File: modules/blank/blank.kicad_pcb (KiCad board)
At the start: 2 copper layers, 27.9 x 66 mm, 2 parts

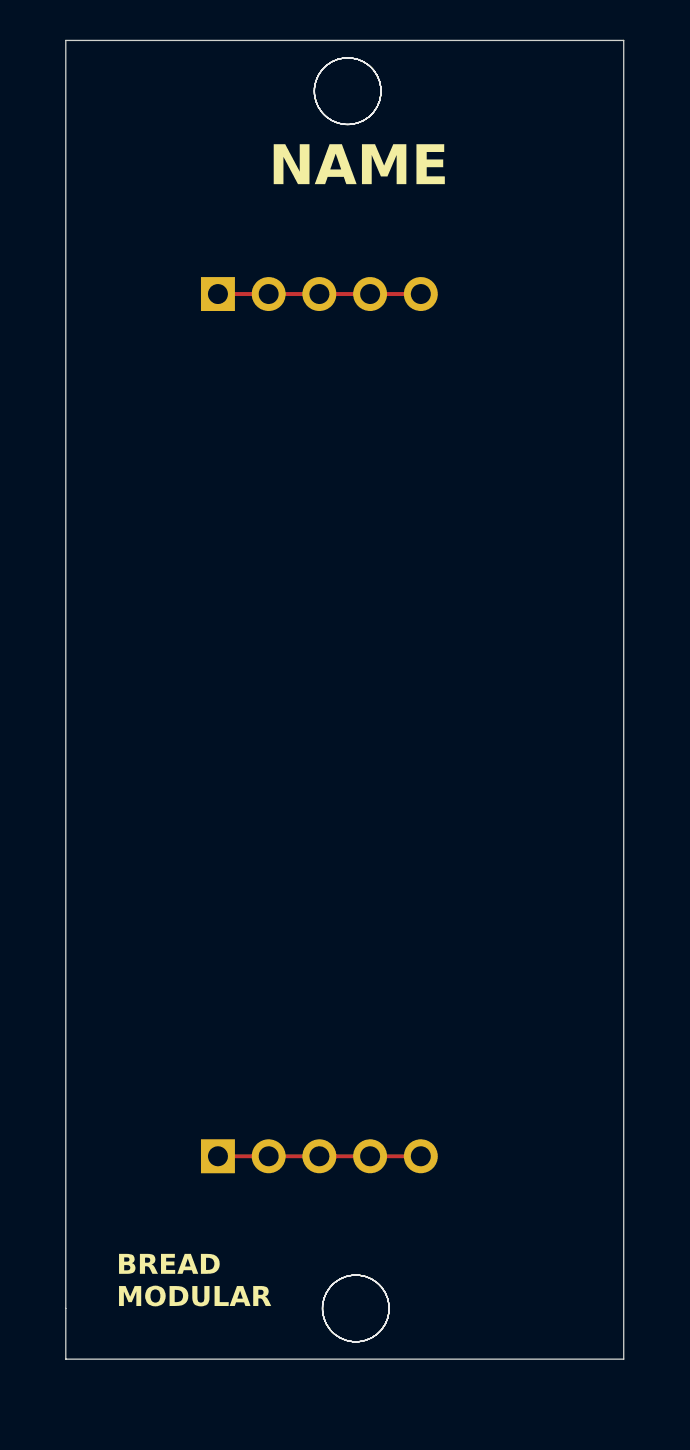
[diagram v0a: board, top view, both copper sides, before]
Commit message: Retouched the Blank Module with new sizes.
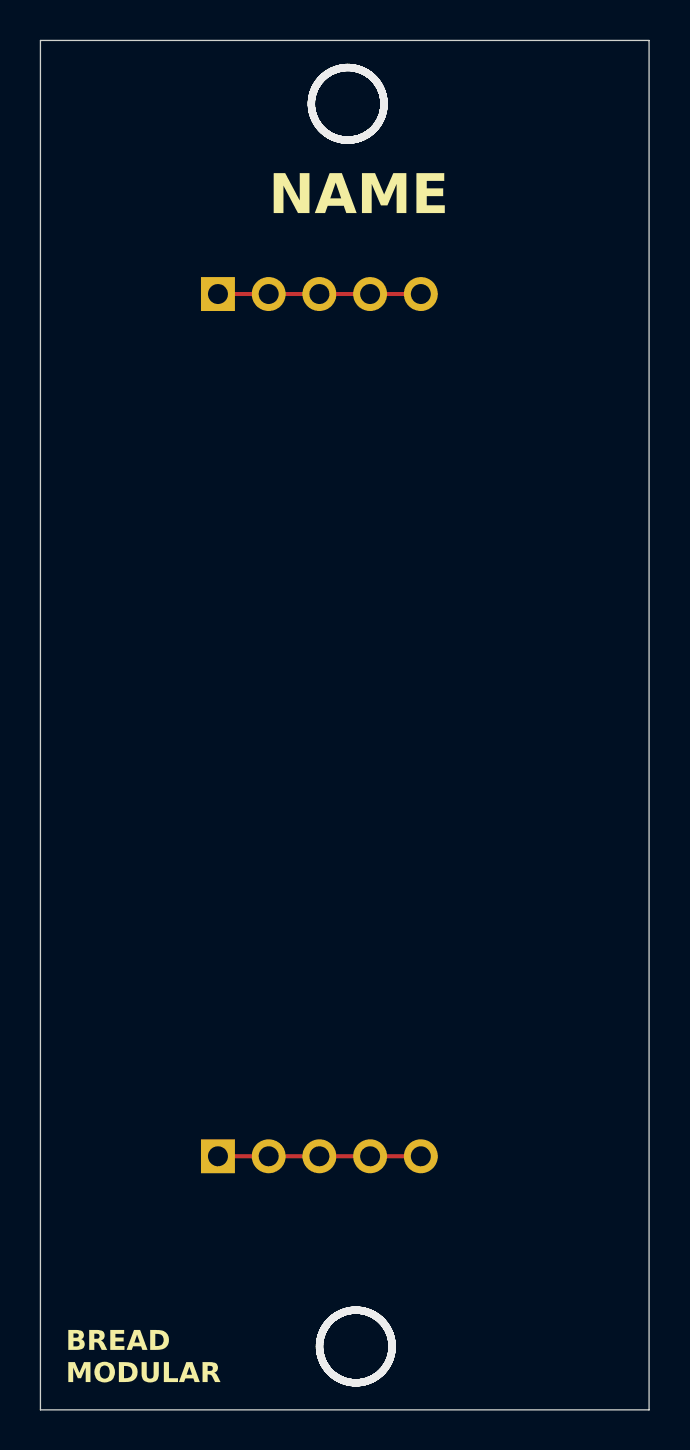
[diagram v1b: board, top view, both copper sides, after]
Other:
- board size 27.9 x 66 mm -> 30.5 x 68.6 mm
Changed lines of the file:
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@@
 	)
 	(gr_line
-		(start 48.26 106.68)
-		(end 76.2 106.68)
+		(start 46.99 109.22)
+		(end 77.47 109.22)
 		(stroke
 			(width 0.05)
@@
 	)
 	(gr_line
-		(start 48.26 104.14)
-		(end 48.26 106.68)
+		(start 77.47 40.64)
+		(end 46.99 40.64)
 		(stroke
 			(width 0.05)
@@
 	)
 	(gr_line
-		(start 76.2 40.64)
-		(end 48.26 40.64)
+		(start 46.99 40.64)
+		(end 46.99 109.22)
 		(stroke
 			(width 0.05)
@@
 	)
 	(gr_line
-		(start 48.26 40.64)
-		(end 48.26 104.14)
-		(stroke
-			(width 0.05)
-			(type default)
-		)
-		(layer "Edge.Cuts")
-	)
-	(gr_line
-		(start 76.2 106.68)
-		(end 76.2 40.64)
+		(start 77.47 109.22)
+		(end 77.47 40.64)
 		(stroke
 			(width 0.05)
@@
 	)
 	(gr_text "NAME"
-		(at 58.42 48.081611 0)
+		(at 58.42 49.53 0)
 		(layer "F.SilkS")
 		(effects
@@
 	)
 	(gr_text "BREAD\nMODULAR"
-		(at 50.8 104.14 0)
+		(at 48.26 107.95 0)
 		(layer "F.SilkS")
 		(effects
@@
 	)
 	(via
-		(at 62.37758 43.18)
-		(size 3.4)
+		(at 62.37758 43.815)
+		(size 4)
 		(drill 3.2)
 		(layers "F.Cu" "B.Cu")
@@
 	)
 	(via
-		(at 62.784908 104.14)
-		(size 3.4)
+		(at 62.784908 106.045)
+		(size 4)
 		(drill 3.2)
 		(layers "F.Cu" "B.Cu")
@@
 	)
 	(via
-		(at 62.37758 43.18)
-		(size 3.4)
+		(at 62.37758 43.815)
+		(size 4)
 		(drill 3.2)
 		(layers "F.Cu" "B.Cu")
@@
 	)
 	(via
-		(at 62.784908 104.14)
-		(size 3.4)
+		(at 62.784908 106.045)
+		(size 4)
 		(drill 3.2)
 		(layers "F.Cu" "B.Cu")
@@
 	)
 	(via
-		(at 62.784908 104.14)
-		(size 3.4)
+		(at 62.784908 106.045)
+		(size 4)
 		(drill 3.2)
 		(layers "F.Cu" "B.Cu")
@@
 	)
 	(via
-		(at 62.784908 104.14)
-		(size 3.4)
+		(at 62.784908 106.045)
+		(size 4)
 		(drill 3.2)
 		(layers "F.Cu" "B.Cu")
@@
 	)
 	(via
-		(at 62.37758 43.18)
-		(size 3.4)
+		(at 62.37758 43.815)
+		(size 4)
 		(drill 3.2)
 		(layers "F.Cu" "B.Cu")
@@
 	)
 	(via
-		(at 62.37758 43.18)
-		(size 3.4)
+		(at 62.37758 43.815)
+		(size 4)
 		(drill 3.2)
 		(layers "F.Cu" "B.Cu")

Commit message: Fixed some pcb layout issues.
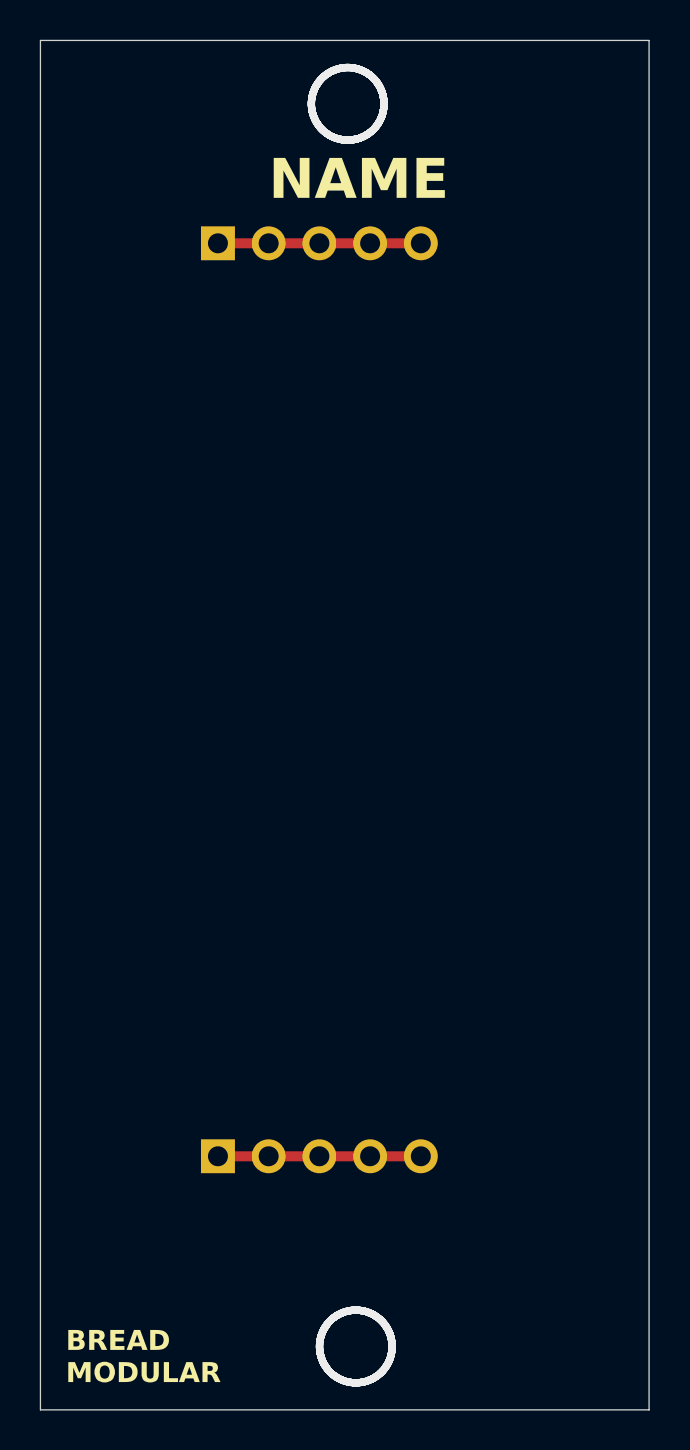
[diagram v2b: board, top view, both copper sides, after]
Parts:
- moved 5V1 2.54 mm to (55.9, 50.8)
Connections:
- 5V1 pad 1: unconnected-(5V1-Pin_1-Pad1) -> Net-(5V1-Pin_1)
- 5V1 pad 2: unconnected-(5V1-Pin_2-Pad2) -> Net-(5V1-Pin_1)
- 5V1 pad 3: unconnected-(5V1-Pin_3-Pad3) -> Net-(5V1-Pin_1)
- 5V1 pad 4: unconnected-(5V1-Pin_4-Pad4) -> Net-(5V1-Pin_1)
- 5V1 pad 5: unconnected-(5V1-Pin_5-Pad5) -> Net-(5V1-Pin_1)
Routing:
- net Net-(5V1-Pin_1): track 0.00 -> 10.2 mm
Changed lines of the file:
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@@
 	(net 0 "")
 	(net 1 "GND")
-	(net 2 "unconnected-(5V1-Pin_4-Pad4)")
-	(net 3 "unconnected-(5V1-Pin_5-Pad5)")
-	(net 4 "unconnected-(5V1-Pin_2-Pad2)")
-	(net 5 "unconnected-(5V1-Pin_3-Pad3)")
-	(net 6 "unconnected-(5V1-Pin_1-Pad1)")
+	(net 2 "Net-(5V1-Pin_1)")
 	(footprint "Connector_PinHeader_2.54mm:PinHeader_1x05_P2.54mm_Vertical"
 		(layer "B.Cu")
@@
 		(property ki_fp_filters "Connector*:*_1x??_*")
 		(sheetname "Root")
-		(sheetfile "buff_mix.kicad_sch")
+		(sheetfile "blank.kicad_sch")
 		(attr through_hole)
 		(fp_line
@@
 	(footprint "Connector_PinHeader_2.54mm:PinHeader_1x05_P2.54mm_Vertical"
 		(layer "B.Cu")
-		(at 55.88 53.34 -90)
+		(at 55.88 50.8 -90)
 		(descr "Through hole straight pin header, 1x05, 2.54mm pitch, single row")
 		(tags "Through hole pin header THT 1x05 2.54mm single row")
@@
 		(property ki_fp_filters "Connector*:*_1x??_*")
 		(sheetname "Root")
-		(sheetfile "buff_mix.kicad_sch")
+		(sheetfile "blank.kicad_sch")
 		(attr through_hole)
 		(fp_line
@@
 			(layers "*.Cu" "*.Mask")
 			(remove_unused_layers no)
-			(net 6 "unconnected-(5V1-Pin_1-Pad1)")
+			(net 2 "Net-(5V1-Pin_1)")
 			(pinfunction "Pin_1")
 			(pintype "passive")
@@
 			(layers "*.Cu" "*.Mask")
 			(remove_unused_layers no)
-			(net 4 "unconnected-(5V1-Pin_2-Pad2)")
+			(net 2 "Net-(5V1-Pin_1)")
 			(pinfunction "Pin_2")
 			(pintype "passive")
@@
 			(layers "*.Cu" "*.Mask")
 			(remove_unused_layers no)
-			(net 5 "unconnected-(5V1-Pin_3-Pad3)")
+			(net 2 "Net-(5V1-Pin_1)")
 			(pinfunction "Pin_3")
 			(pintype "passive")
@@
 			(layers "*.Cu" "*.Mask")
 			(remove_unused_layers no)
-			(net 2 "unconnected-(5V1-Pin_4-Pad4)")
+			(net 2 "Net-(5V1-Pin_1)")
 			(pinfunction "Pin_4")
 			(pintype "passive")
@@
 			(layers "*.Cu" "*.Mask")
 			(remove_unused_layers no)
-			(net 3 "unconnected-(5V1-Pin_5-Pad5)")
+			(net 2 "Net-(5V1-Pin_1)")
 			(pinfunction "Pin_5")
 			(pintype "passive")
@@
 			)
 		)
-	)
-	(gr_line
-		(start 55.88 53.34)
-		(end 66.04 53.34)
-		(stroke
-			(width 0.2)
-			(type default)
-		)
-		(layer "F.Cu")
 	)
 	(gr_line
@@
 	)
 	(gr_text "NAME"
-		(at 58.42 49.53 0)
+		(at 58.42 48.768 0)
 		(layer "F.SilkS")
 		(effects
@@
 	)
 	(segment
-		(start 58.42 96.52)
+		(start 55.88 96.52)
 		(end 66.04 96.52)
-		(width 0.2)
+		(width 0.5)
 		(layer "F.Cu")
 		(net 1)
 	)
 	(segment
-		(start 55.88 96.52)
-		(end 58.42 96.52)
-		(width 0.2)
+		(start 55.88 50.8)
+		(end 66.04 50.8)
+		(width 0.5)
 		(layer "F.Cu")
-		(net 1)
+		(net 2)
 	)
 )

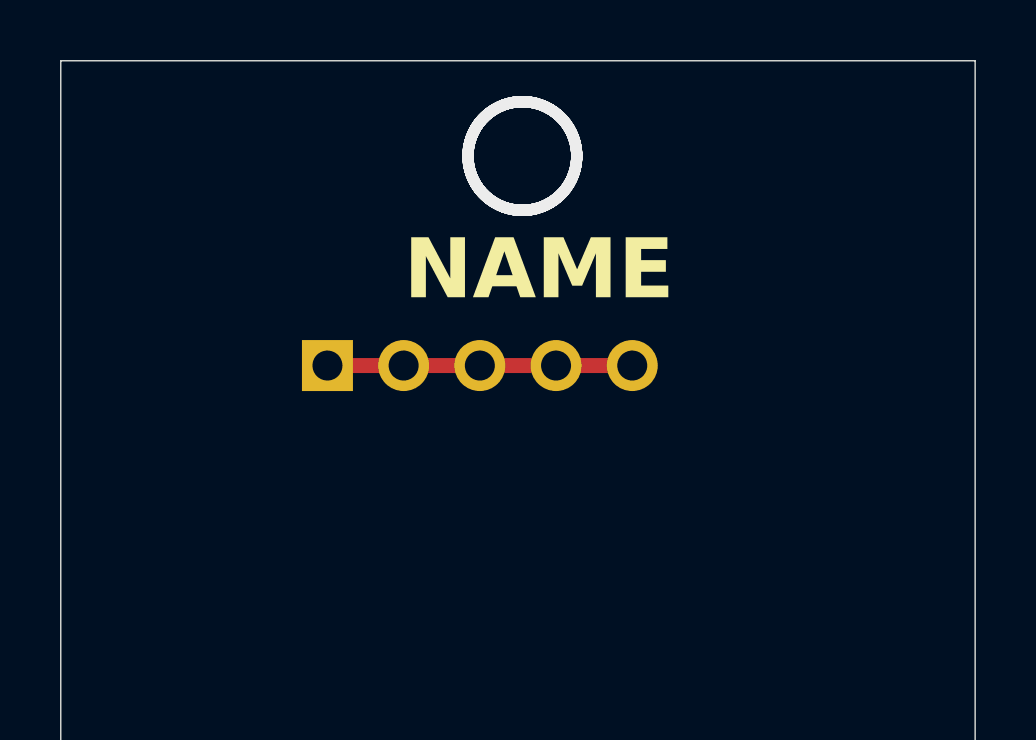
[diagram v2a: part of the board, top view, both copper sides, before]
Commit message: Add sockets for the blank project.
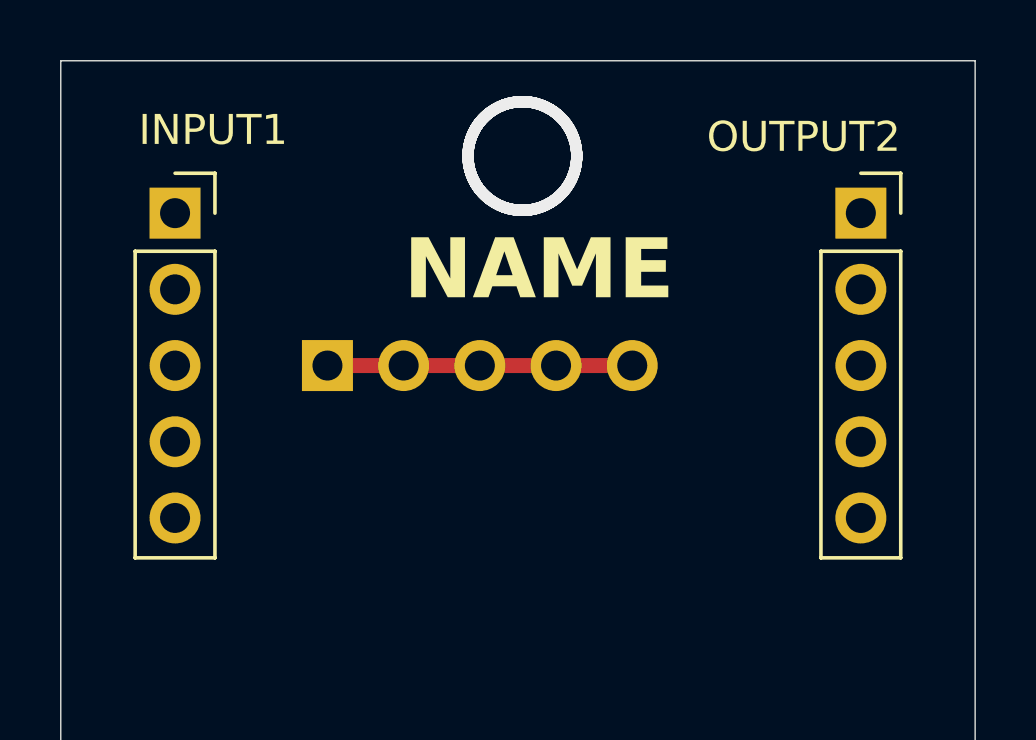
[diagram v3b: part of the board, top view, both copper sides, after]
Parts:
- added INPUT1: Conn_01x05_Socket, Connector_PinSocket_2.54mm:PinSocket_1x05_P2.54mm_Vertical, F.Cu at (50.8, 45.7)
- added OUTPUT2: Conn_01x05_Socket, Connector_PinSocket_2.54mm:PinSocket_1x05_P2.54mm_Vertical, F.Cu at (73.7, 45.7)

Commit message: Update the basic kidcad app Add simulation support Introduce the version number silkscreen
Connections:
- net Net-(5V1-Pin_1) renamed +5V
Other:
- board text added: "NAME 0.0.0"
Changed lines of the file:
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@@
 	(net 0 "")
 	(net 1 "GND")
-	(net 2 "Net-(5V1-Pin_1)")
+	(net 2 "+5V")
 	(net 3 "unconnected-(INPUT1-Pin_3-Pad3)")
 	(net 4 "unconnected-(INPUT1-Pin_4-Pad4)")
@@
 			(layers "*.Cu" "*.Mask")
 			(remove_unused_layers no)
-			(net 2 "Net-(5V1-Pin_1)")
+			(net 2 "+5V")
 			(pinfunction "Pin_1")
 			(pintype "passive")
@@
 			(layers "*.Cu" "*.Mask")
 			(remove_unused_layers no)
-			(net 2 "Net-(5V1-Pin_1)")
+			(net 2 "+5V")
 			(pinfunction "Pin_2")
 			(pintype "passive")
@@
 			(layers "*.Cu" "*.Mask")
 			(remove_unused_layers no)
-			(net 2 "Net-(5V1-Pin_1)")
+			(net 2 "+5V")
 			(pinfunction "Pin_3")
 			(pintype "passive")
@@
 			(layers "*.Cu" "*.Mask")
 			(remove_unused_layers no)
-			(net 2 "Net-(5V1-Pin_1)")
+			(net 2 "+5V")
 			(pinfunction "Pin_4")
 			(pintype "passive")
@@
 			(layers "*.Cu" "*.Mask")
 			(remove_unused_layers no)
-			(net 2 "Net-(5V1-Pin_1)")
+			(net 2 "+5V")
 			(pinfunction "Pin_5")
 			(pintype "passive")
@@
 		(layer "Edge.Cuts")
 	)
+	(gr_text "NAME\n0.0.0"
+		(at 76.327 107.95 0)
+		(layer "F.SilkS")
+		(effects
+			(font
+				(size 1 1)
+				(thickness 0.2)
+				(bold yes)
+			)
+			(justify right bottom)
+		)
+	)
 	(gr_text "NAME"

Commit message: Update the blank module.
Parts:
- removed 5V1: Conn_01x05_Pin, Connector_PinHeader_2.54mm:PinHeader_1x05_P2.54mm_Vertical
- removed OUTPUT2: Conn_01x05_Socket, Connector_PinSocket_2.54mm:PinSocket_1x05_P2.54mm_Vertical
- added OUTPUT1: Conn_01x05_Socket, Connector_PinSocket_2.54mm:PinSocket_1x05_P2.54mm_Vertical, F.Cu at (73.7, 45.7)
- added V_SUPPLY1: Conn_01x05_Pin, BreadModular_MISC:Power_Connector, B.Cu at (55.9, 50.8)
- GND1: footprint Connector_PinHeader_2.54mm:PinHeader_1x05_P2.54mm_Vertical -> BreadModular_MISC:Power_Connector
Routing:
- net V_SUPPLY: track 0.00 -> 10.2 mm
- net +5V: track 10.2 -> 0.00 mm
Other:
- board text added: "INPUT"
- board text added: "OUTPUT"

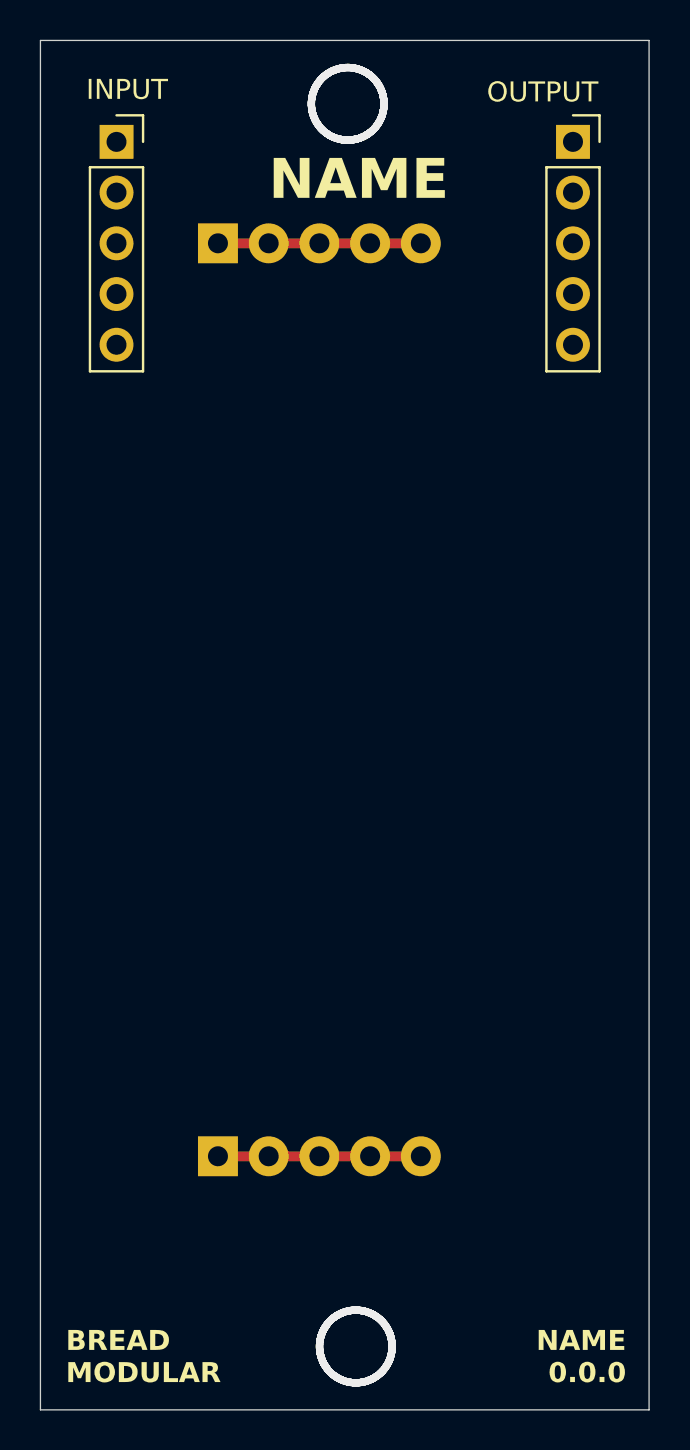
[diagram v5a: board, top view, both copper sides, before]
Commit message: blank:Add opamp & pot as a built-in components These are used in almost all the projects. So, having pre-build components make is easy to get started
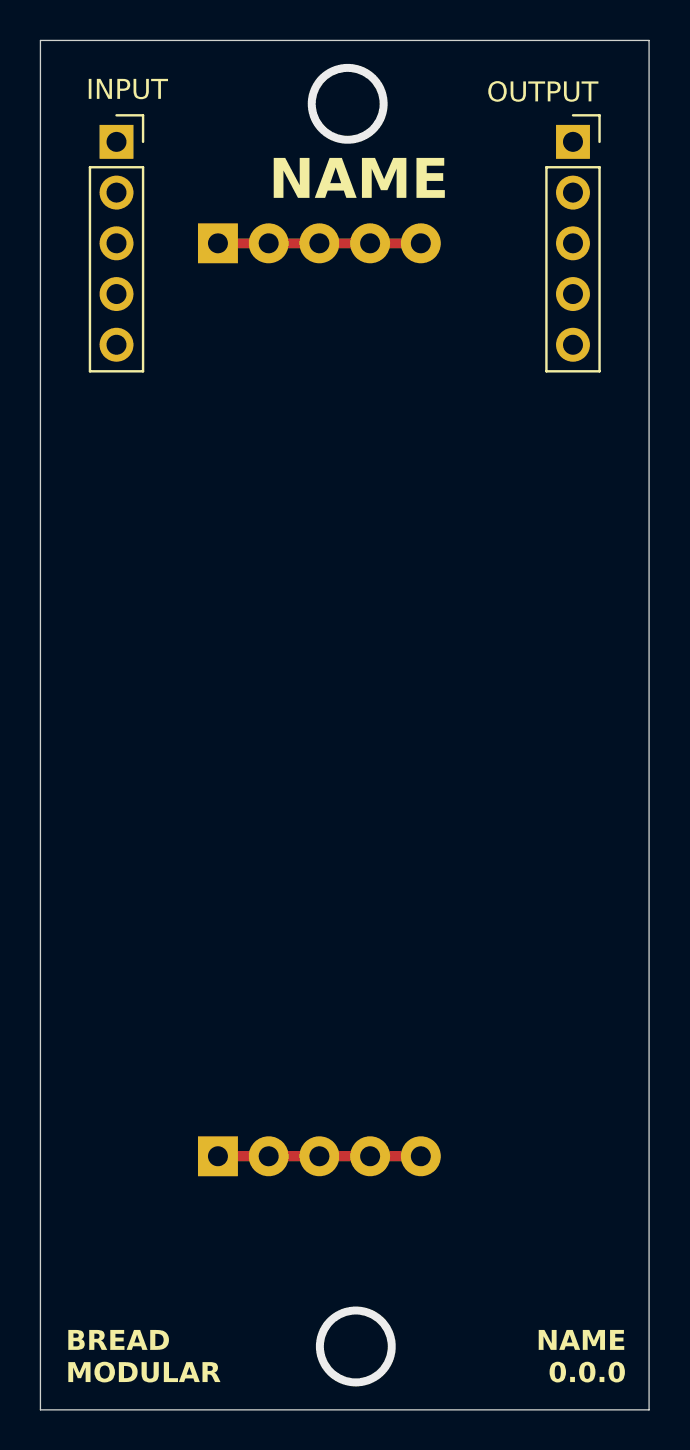
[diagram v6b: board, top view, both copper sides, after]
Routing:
- net (no net): vias 8 -> 2
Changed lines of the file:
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@@
 		)
 		(fp_text user "${REFERENCE}"
-			(at 0 -5.08 360)
+			(at 0 -5.08 0)
 			(layer "B.Fab")
 			(effects
@@
 	)
 	(via
-		(at 62.37758 43.815)
-		(size 4)
-		(drill 3.2)
-		(layers "F.Cu" "B.Cu")
-		(net 0)
-	)
-	(via
 		(at 62.784908 106.045)
 		(size 4)
 		(drill 3.2)
-		(layers "F.Cu" "B.Cu")
-		(net 0)
-	)
-	(via
-		(at 62.37758 43.815)
-		(size 4)
-		(drill 3.2)
-		(layers "F.Cu" "B.Cu")
-		(net 0)
-	)
-	(via
-		(at 62.784908 106.045)
-		(size 4)
-		(drill 3.2)
-		(layers "F.Cu" "B.Cu")
-		(net 0)
-	)
-	(via
-		(at 62.784908 106.045)
-		(size 4)
-		(drill 3.2)
-		(layers "F.Cu" "B.Cu")
-		(net 0)
-	)
-	(via
-		(at 62.784908 106.045)
-		(size 4)
-		(drill 3.2)
-		(layers "F.Cu" "B.Cu")
-		(net 0)
-	)
-	(via
-		(at 62.37758 43.815)
-		(size 4)
-		(drill 3.2)
